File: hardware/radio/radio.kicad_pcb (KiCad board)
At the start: 4 copper layers, 35 x 35 mm, 49 parts, among them IC301 ATMEGA328-P, P101 CONN_01X04, P102 CONN_02X03, P103 CONN_02X05, P104 CONN_01X02, Q301 Q_NMOS_DGS, U201 LTC3331, X301 8MHz

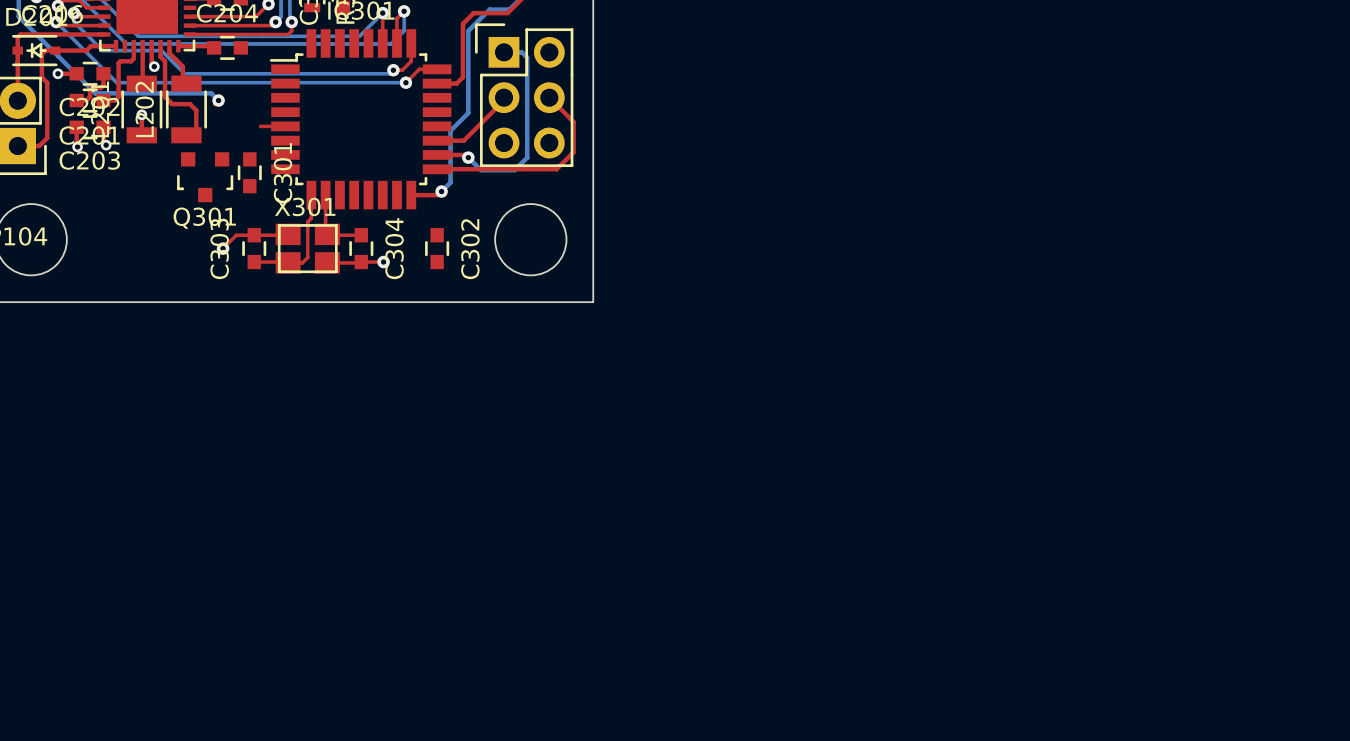
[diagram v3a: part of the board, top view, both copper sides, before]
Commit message: Associate battery, BLE113, OR-gate, ADXL375 footprints
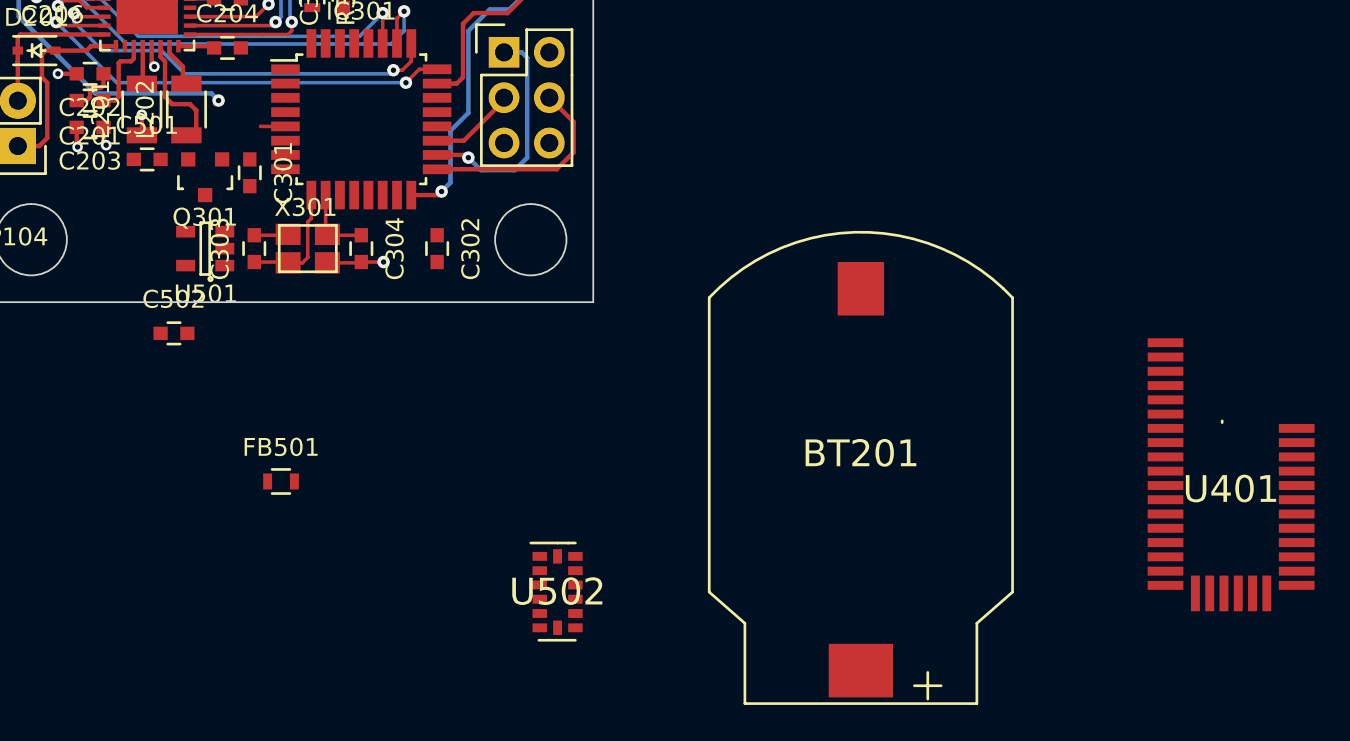
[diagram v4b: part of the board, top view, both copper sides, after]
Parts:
- added BT201: Battery, footprints:CR2032-holder-S8421R, F.Cu at (125.0, 117.8)
- added C501: 100n, Capacitors_SMD:C_0603, F.Cu at (85.0, 102.0)
- added C502: 100n, Capacitors_SMD:C_0603, F.Cu at (86.5, 111.8)
- added FB501: FILTER, Resistors_SMD:R_0603, F.Cu at (92.5, 120.1)
- added U401: BLE113, footprints:BLE113, F.Cu at (145.8, 119.8)
- added U501: SN74AUP1T32, Housings_SOT-23_SOT-143_TSOT-6:SOT-23-5, F.Cu at (88.2, 107.0)
- added U502: ADXL375, footprints:LGA-14_(CC-14-1), F.Cu at (108.0, 126.2)
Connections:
- IC301 pad 15: /Control/SPI_SS -> /Sensor/CS
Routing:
- net GND: track 10.9 -> 8.62 mm, vias 5 -> 4

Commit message: Work on PCB
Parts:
- BT201: moved to B.Cu
- IC301: value ATMEGA328-P -> ATMEGA328-A
- moved U401 67.7 mm to (92.5, 78.0)
- moved BT201 39.3 mm to (93.0, 95.0)
- moved U502 30.3 mm to (85.5, 106.0)
- moved C401 18.9 mm to (105.0, 90.2), turned to 270 degrees
- moved FB501 18.4 mm to (82.8, 104.5), turned to 270 degrees
- moved R214 9.83 mm to (89.5, 93.2), turned to 0 degrees
- moved R202 8.76 mm to (77.8, 92.2), turned to 0 degrees
- moved R217 8.70 mm to (91.0, 93.2), turned to 0 degrees
- moved R215 8.02 mm to (89.5, 91.5), turned to 0 degrees
- moved R205 7.52 mm to (79.2, 92.2), turned to 0 degrees
- moved R203 7.11 mm to (77.8, 90.5), turned to 0 degrees
- moved C402 6.73 mm to (86.5, 84.5), turned to 270 degrees
- moved R216 6.64 mm to (89.5, 89.8), turned to 0 degrees
- moved R218 6.58 mm to (91.0, 91.5), turned to 0 degrees
- moved C207 6.05 mm to (94.8, 90.0)
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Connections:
- IC301 pad 1: /Control/RESET -> /Control/INT1
- IC301 pad 10: Net-(C304-Pad1) -> Net-(IC301-Pad10)
- IC301 pad 11: Net-(D301-Pad2) -> Net-(IC301-Pad11)
- IC301 pad 13: Net-(IC301-Pad13) -> /Sensor/CS
- IC301 pad 14: Net-(IC301-Pad14) -> /Control/SW_RX
- IC301 pad 15: /Sensor/CS -> /Control/MOSI
- IC301 pad 16: /Control/SW_RX -> /Control/MISO
- IC301 pad 17: /Control/MOSI -> /Control/SCK
- IC301 pad 18: /Control/MISO -> VCC
- IC301 pad 19: /Control/SCK -> Net-(IC301-Pad19)
- IC301 pad 2: /Control/RX -> /Control/BLE_RS
- IC301 pad 20: VCC -> Net-(C302-Pad1)
- IC301 pad 21: Net-(C302-Pad1) -> GND
- IC301 pad 22: GND -> Net-(IC301-Pad22)
- IC301 pad 29: (no net) -> /Control/RESET
- IC301 pad 3: /Bluetooth/RXD -> GND
- IC301 pad 30: (no net) -> /Control/RX
- IC301 pad 31: (no net) -> /Bluetooth/RXD
- IC301 pad 32: (no net) -> /Control/INT0
- IC301 pad 4: /Control/INT0 -> VCC
- IC301 pad 5: /Control/INT1 -> GND
- IC301 pad 6: /Control/BLE_RS -> VCC
- IC301 pad 7: VCC -> Net-(C303-Pad1)
- IC301 pad 8: GND -> Net-(C304-Pad1)
- IC301 pad 9: Net-(C303-Pad1) -> Net-(D301-Pad2)
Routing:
- net /Power management/VIN3: track 35.2 -> 0.00 mm
- net /Control/UV3: track 27.2 -> 0.00 mm, vias 2 -> 0
- net /Control/UV2: track 27.0 -> 0.00 mm, vias 2 -> 0
- net /Power management/IPK1: track 26.4 -> 0.00 mm, vias 2 -> 0
- net /Power management/IPK0: track 26.4 -> 0.00 mm, vias 2 -> 0
- net /Control/UV0: track 25.9 -> 0.00 mm, vias 2 -> 0
- net /Control/EH_ON: track 25.7 -> 0.00 mm, vias 2 -> 0
- net /Power management/IPK2: track 25.5 -> 0.00 mm, vias 2 -> 0
- net /Control/SW_RX: track 25.4 -> 0.00 mm, vias 1 -> 0
- net /Control/UV1: track 23.7 -> 0.00 mm, vias 2 -> 0
- net /Control/SW_TX: track 16.6 -> 0.00 mm
- net /Control/MISO: track 12.7 -> 0.00 mm, vias 1 -> 0
- net /Power management/OUT2: track 12.4 -> 0.00 mm
- net /Power management/OUT1: track 12.2 -> 0.00 mm
- net /Control/MOSI: track 11.7 -> 0.00 mm
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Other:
- board size 35 x 35 mm -> 35 x 41 mm

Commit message: Start routing the PCB
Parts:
- moved C302 14.8 mm to (97.6, 92.7), turned to 90 degrees
- moved Q301 9.33 mm to (93.0, 107.0)
- moved C303 5.00 mm to (96.0, 107.0)
- moved C304 5.00 mm to (102.0, 107.0)
- moved X301 5.00 mm to (99.0, 107.0)
- moved R202 4.22 mm to (77.0, 88.1), turned to 270 degrees
- moved U501 3.77 mm to (89.4, 107.0)
- moved R205 3.48 mm to (77.0, 89.6), turned to 270 degrees
- moved R204 2.83 mm to (80.5, 88.1), turned to 270 degrees
- moved R203 2.60 mm to (78.8, 88.1), turned to 270 degrees
- moved C206 2.39 mm to (79.4, 91.7)
- moved BT201 2.11 mm to (92.8, 92.9)
- moved R214 2.11 mm to (89.3, 91.2)
- moved R215 2.11 mm to (89.3, 89.4)
- moved R216 2.11 mm to (89.3, 87.7)
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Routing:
- net /Power management/IPK2: track 0.00 -> 30.2 mm, vias 0 -> 2
- net /Power management/IPK1: track 0.00 -> 25.6 mm, vias 0 -> 2
- net /Power management/VIN3: track 0.00 -> 24.6 mm
- net Net-(C204-Pad1): track 0.00 -> 22.0 mm, vias 0 -> 3
- net GND: track 0.00 -> 21.6 mm, vias 0 -> 14
- net /Power management/IPK0: track 0.00 -> 17.3 mm, vias 0 -> 2
- net /Control/INT0: track 0.00 -> 10.1 mm
- net /Power management/Harvest2: track 0.00 -> 10.1 mm
- net /Sensor/CS: track 0.00 -> 9.49 mm
- net Net-(BT201-Pad1): track 0.00 -> 9.42 mm
- net VCC: track 0.00 -> 7.61 mm, vias 0 -> 3
- net /Power management/FLOAT0: track 0.00 -> 7.59 mm
- net /Power management/Harvest1: track 0.00 -> 7.54 mm
- net /Power management/OUT2: track 0.00 -> 7.13 mm
- net /Power management/OUT1: track 0.00 -> 6.15 mm
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
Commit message: Assign testpoint footprints
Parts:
- added C306: C, Capacitors_SMD:C_0603, F.Cu at (92.5, 120.1)
- added R1: R, Resistors_SMD:R_0603, F.Cu at (100.0, 120.0)
- added R2: R, Resistors_SMD:R_0603, F.Cu at (88.0, 121.0)
- added R3: R, Resistors_SMD:R_0603, F.Cu at (96.5, 121.5)
- added R4: R, Resistors_SMD:R_0603, F.Cu at (91.8, 122.5)
- added R5: R, Resistors_SMD:R_0603, F.Cu at (104.0, 120.8)
- added R6: R, Resistors_SMD:R_0603, F.Cu at (101.2, 122.5)
- added W1, W2, W201, W3, W4, W7, W9: TEST, footprints_:Test_pair_TH_small, F.Cu at (92.5, 120.1)
- added W5, W6, W8: TEST, footprints_:Test_pair_TH_tiny, F.Cu at (92.5, 120.1)
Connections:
- BT201 pad 2: GND -> Net-(BT201-Pad2)
- C203 pad 1: VCC -> /Power management/VOUT
- C207 pad 1: Net-(BT201-Pad1) -> Net-(C207-Pad1)
- L201 pad 1: VCC -> /Power management/VOUT
- U201 pad 13: VCC -> /Power management/VOUT
- U201 pad 21: Net-(BT201-Pad1) -> Net-(C207-Pad1)
- U201 pad 8: /Power management/Harvest1 -> Net-(R5-Pad1)
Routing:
- net Net-(C207-Pad1): track 0.00 -> 9.42 mm
- net Net-(BT201-Pad1): track 9.42 -> 0.00 mm
- net VCC: track 7.61 -> 4.39 mm, vias 3 -> 2
- net /Power management/VOUT: track 0.00 -> 3.22 mm, vias 0 -> 1
- net Net-(R5-Pad1): track 0.00 -> 0.90 mm
- net /Power management/Harvest1: track 7.54 -> 6.64 mm

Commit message: Continue on TP layout
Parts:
- moved R5 37.5 mm to (77.8, 94.0), turned to 180 degrees
- moved R1 26.0 mm to (81.5, 101.8)
- moved R2 22.6 mm to (90.0, 98.5)
- moved C401 21.8 mm to (84.0, 84.2), turned to 180 degrees
- moved W1 19.8 mm to (81.2, 103.8), turned to 180 degrees
- moved R302 17.7 mm to (107.2, 101.5), turned to 180 degrees
- moved W3 16.1 mm to (91.8, 104.0), turned to 180 degrees
- moved D301 13.3 mm to (107.2, 99.8), turned to 180 degrees
- moved P102 12.0 mm to (104.8, 84.0)
- moved P101 9.22 mm to (101.0, 78.0)
- moved W2 7.30 mm to (92.5, 112.8)
- moved IC301 3.64 mm to (98.0, 96.5)
- moved R401 3.50 mm to (100.0, 89.2)
- moved C305 2.75 mm to (96.0, 90.0)
- moved R301 2.75 mm to (94.2, 90.0)
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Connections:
- C301 pad 1: VCC -> /Control/VCC_uc
- C306 pad 1: VCC -> /Control/VCC_uc
- C401 pad 1: VCC -> /Bluetooth/VCC_BLE
- C402 pad 1: VCC -> /Bluetooth/VCC_BLE
- C403 pad 1: VCC -> /Bluetooth/VCC_BLE
- C501 pad 1: VCC -> /Sensor/VCC_ACC
- FB501 pad 1: VCC -> /Sensor/VCC_ACC
- IC301 pad 18: VCC -> /Control/VCC_uc
- IC301 pad 4: VCC -> /Control/VCC_uc
- IC301 pad 6: VCC -> /Control/VCC_uc
- P102 pad 2: VCC -> /Control/VCC_uc
- P103 pad 1: VCC -> /Bluetooth/VCC_BLE
- R2 pad 1: VCC -> /Control/VCC_uc
- R3 pad 1: VCC -> /Sensor/VCC_ACC
- R4 pad 1: VCC -> /Bluetooth/VCC_BLE
- R401 pad 1: VCC -> /Bluetooth/VCC_BLE
- U401 pad 17: VCC -> /Bluetooth/VCC_BLE
- U401 pad 8: VCC -> /Bluetooth/VCC_BLE
- U502 pad 1: VCC -> /Sensor/VCC_ACC
- W2 pad 2: VCC -> /Control/VCC_uc
- W3 pad 2: VCC -> /Sensor/VCC_ACC
- W4 pad 2: VCC -> /Bluetooth/VCC_BLE
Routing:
- net /Power management/VOUT: track 3.22 -> 8.66 mm
- net Net-(C207-Pad1): track 9.42 -> 5.08 mm
- net Net-(R5-Pad1): track 0.90 -> 4.66 mm
- net /Sensor/VCC_ACC: track 0.00 -> 3.21 mm, vias 0 -> 1
- net /Power management/Harvest1: track 6.64 -> 5.31 mm
- net GND: track 21.6 -> 20.4 mm, vias 14 -> 13
- net VCC: track 4.39 -> 4.46 mm, vias 2 -> 1
